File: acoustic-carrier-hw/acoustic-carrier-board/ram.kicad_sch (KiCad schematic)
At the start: 15 parts, among them IC1 ECP5-BGA256, IC2 MT41K256M16TW-107_P

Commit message: [carrier] Fixed minor symbol errors, added minor routing info (next) continue schematic check
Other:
- moved on the sheet: R54
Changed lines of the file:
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@@
 	(wire
 		(pts
-			(xy 223.52 68.58) (xy 227.33 68.58)
+			(xy 223.52 68.58) (xy 228.6 68.58)
 		)
 		(stroke
@@
 	(wire
 		(pts
-			(xy 232.41 68.58) (xy 240.03 68.58)
+			(xy 233.68 68.58) (xy 240.03 68.58)
 		)
 		(stroke
@@
 		(on_board yes)
 		(dnp no)
-		(fields_autoplaced yes)
 		(property "Reference" "IC1"
-			(at 90.17 76.6942 0)
+			(at 97.282 85.598 0)
 			(effects
 				(font
@@
 		)
 		(property "Value" "ECP5-BGA256"
-			(at 90.17 79.2342 0)
+			(at 106.426 88.392 0)
 			(effects
 				(font
@@
 	(symbol
 		(lib_id "Device:R_Small")
-		(at 229.87 68.58 90)
+		(at 231.14 68.58 90)
 		(unit 1)
 		(exclude_from_sim no)
@@
 		(dnp no)
 		(property "Reference" "R54"
-			(at 229.362 70.612 90)
+			(at 230.632 70.612 90)
 			(effects
 				(font
@@
 		)
 		(property "Value" "240"
-			(at 225.806 69.85 90)
+			(at 227.076 69.85 90)
 			(effects
 				(font
@@
 		)
 		(property "Footprint" "Resistor_SMD:R_0603_1608Metric"
-			(at 229.87 68.58 0)
+			(at 231.14 68.58 0)
 			(effects
 				(font
@@
 			)
 		)
-		(property "Datasheet" "~"
-			(at 229.87 68.58 0)
+		(property "Datasheet" "https://jlcpcb.com/api/file/downloadByFileSystemAccessId/8579706336479019008"
+			(at 231.14 68.58 0)
 			(effects
 				(font
@@
 		)
 		(property "Description" "Resistor, small symbol"
-			(at 229.87 68.58 0)
+			(at 231.14 68.58 0)
 			(effects
 				(font
@@
 		)
 		(property "LPN" "0603WAF2400T5E"
-			(at 229.87 68.58 0)
+			(at 231.14 68.58 0)
 			(effects
 				(font
@@
 		)
 		(property "MPN" "C23350"
-			(at 229.87 68.58 0)
-			(effects
-				(font
-					(size 1.27 1.27)
-				)
-				(hide yes)
-			)
-		)
-		(property "Part Number" ""
-			(at 229.87 68.58 90)
-			(effects
-				(font
-					(size 1.27 1.27)
-				)
-				(hide yes)
-			)
-		)
-		(property "SN-DK" ""
-			(at 229.87 68.58 90)
-			(effects
-				(font
-					(size 1.27 1.27)
-				)
-				(hide yes)
-			)
-		)
-		(property "Sim.Pin" ""
-			(at 229.87 68.58 90)
-			(effects
-				(font
-					(size 1.27 1.27)
-				)
-				(hide yes)
-			)
-		)
-		(property "LCSC Part" ""
-			(at 229.87 68.58 90)
+			(at 231.14 68.58 0)
 			(effects
 				(font

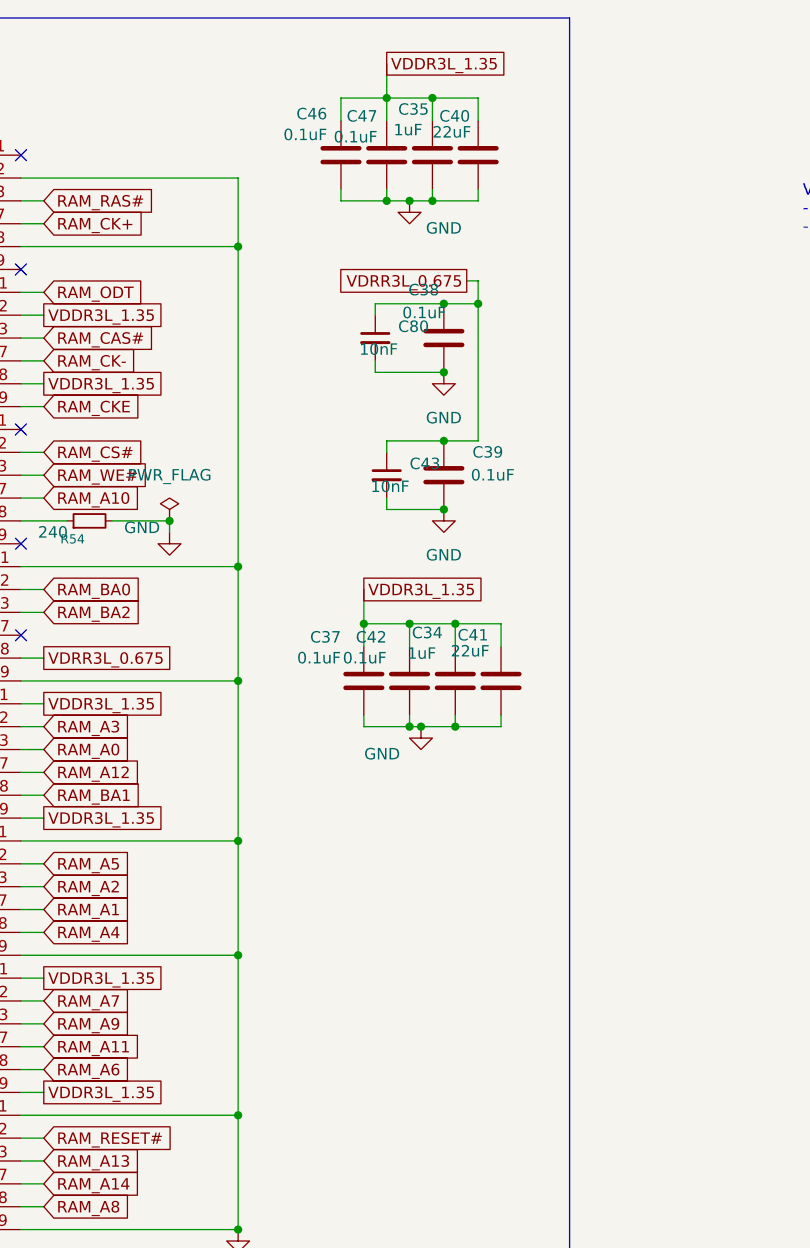
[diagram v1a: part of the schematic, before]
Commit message: [carrier] Finished flash and config check
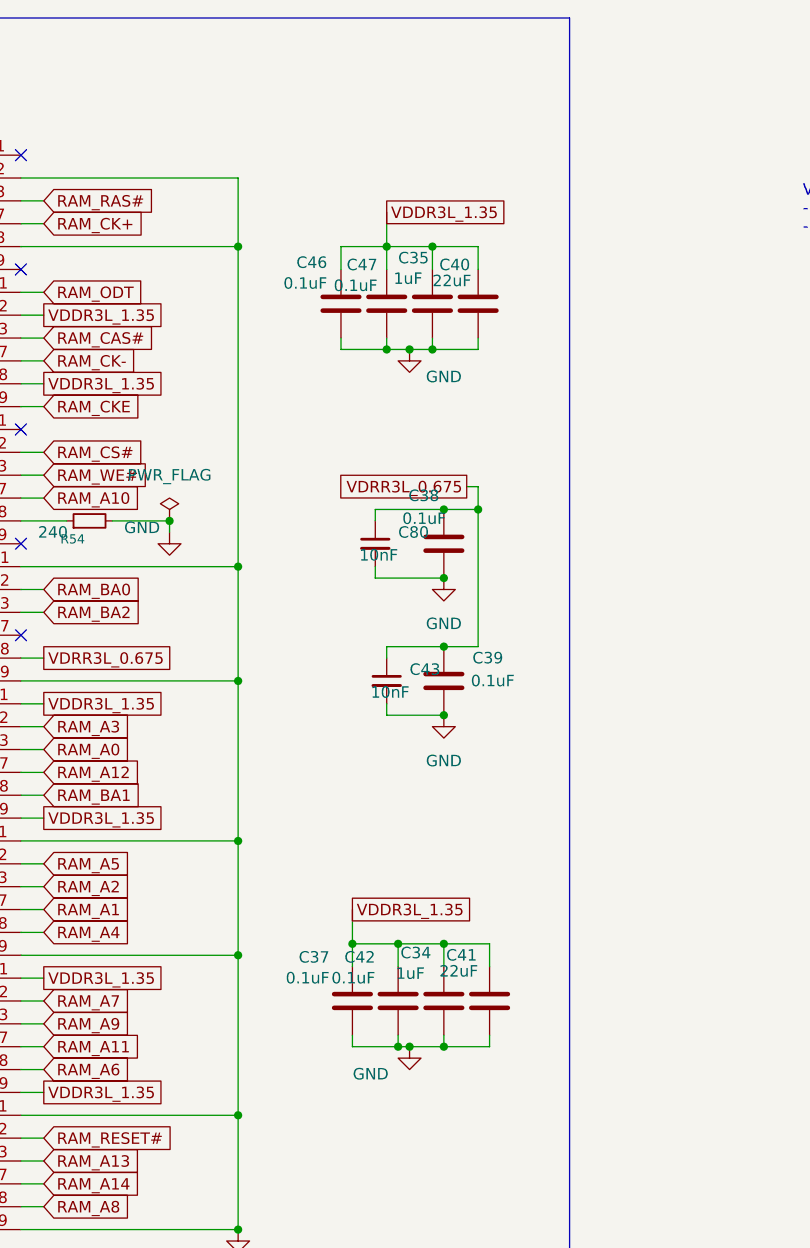
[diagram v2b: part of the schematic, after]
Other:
- moved on the sheet: C34, C35, C37, C38, C39, C40, C41, C42, C43, C46, C47, C80

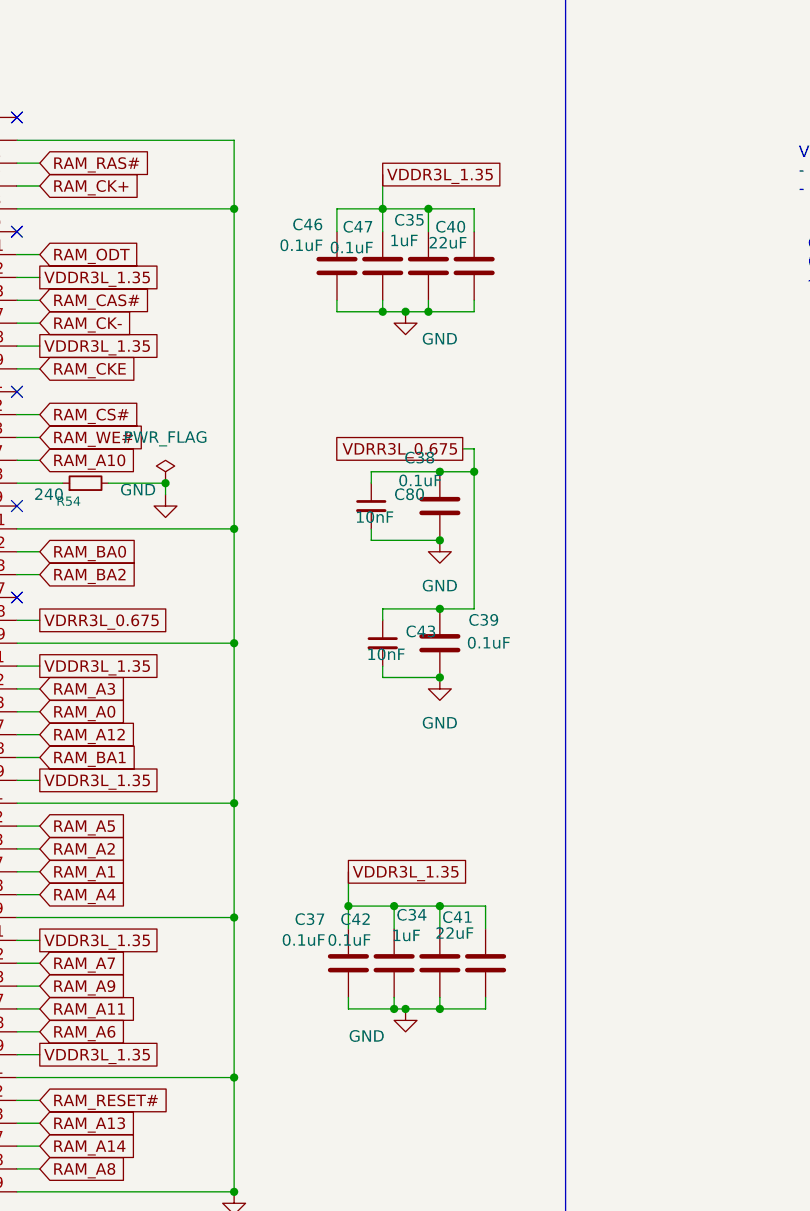
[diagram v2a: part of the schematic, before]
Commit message: [carrier] Further verification of power board (next) Replace ddr3l reference voltage using TPS51200
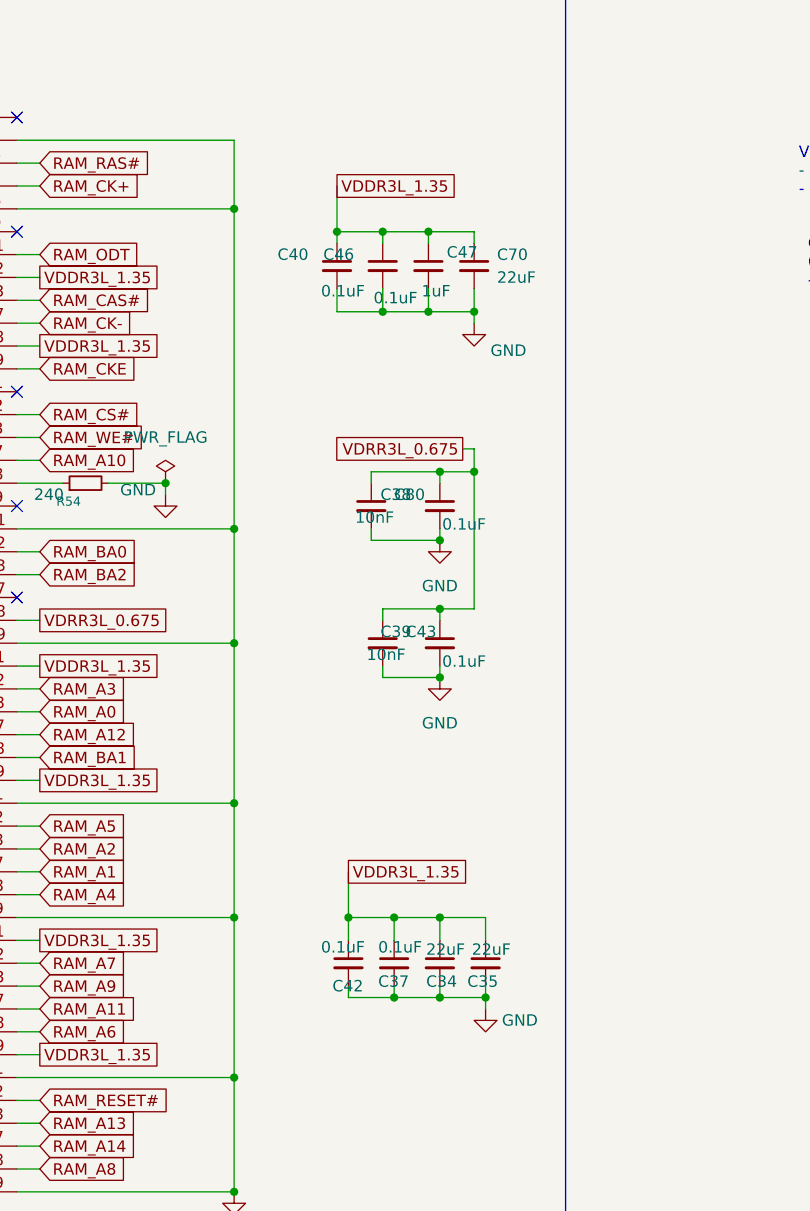
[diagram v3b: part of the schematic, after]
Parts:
- removed C34, C35: 1uF, Capacitor_SMD:C_0805_2012Metric, symbol Device:C
- removed C37, C38, C39, C42, C46, C47: 0.1uF, Capacitor_SMD:C_0402_1005Metric, symbol Device:C
- removed C40, C41: 22uF, Capacitor_SMD:C_0603_1608Metric, symbol Device:C
- added C34, C35, C70: 22uF, Capacitor_SMD:C_0603_1608Metric, symbol Device:C_Small
- added C37, C38, C39, C40, C42, C46: 0.1uF, Capacitor_SMD:C_0402_1005Metric, symbol Device:C_Small
- added C47: 1uF, Capacitor_SMD:C_0805_2012Metric, symbol Device:C_Small
- IC2: Height 1.2 -> (none); Manufacturer_Name Micron -> (none); Manufacturer_Part_Number MT41K256M16TW-107:P -> (none); Mouser Part Number 340-265846-TRAY -> (none); Mouser Price/Stock https://www.mouser.co.uk/ProductDetail/Micron/MT41K256M16TW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 -> (none)
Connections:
- net GND: now also C34.2, C35.2, C37.2, C38.2, C39.2, C40.2, C42.2, C46.2, C47.2, C70.2
- net VDDR3L_1.35: now also C34.1, C35.1, C37.1, C40.1, C42.1, C46.1, C47.1, C70.1
- net VDRR3L_0.675: now also C38.1, C39.1

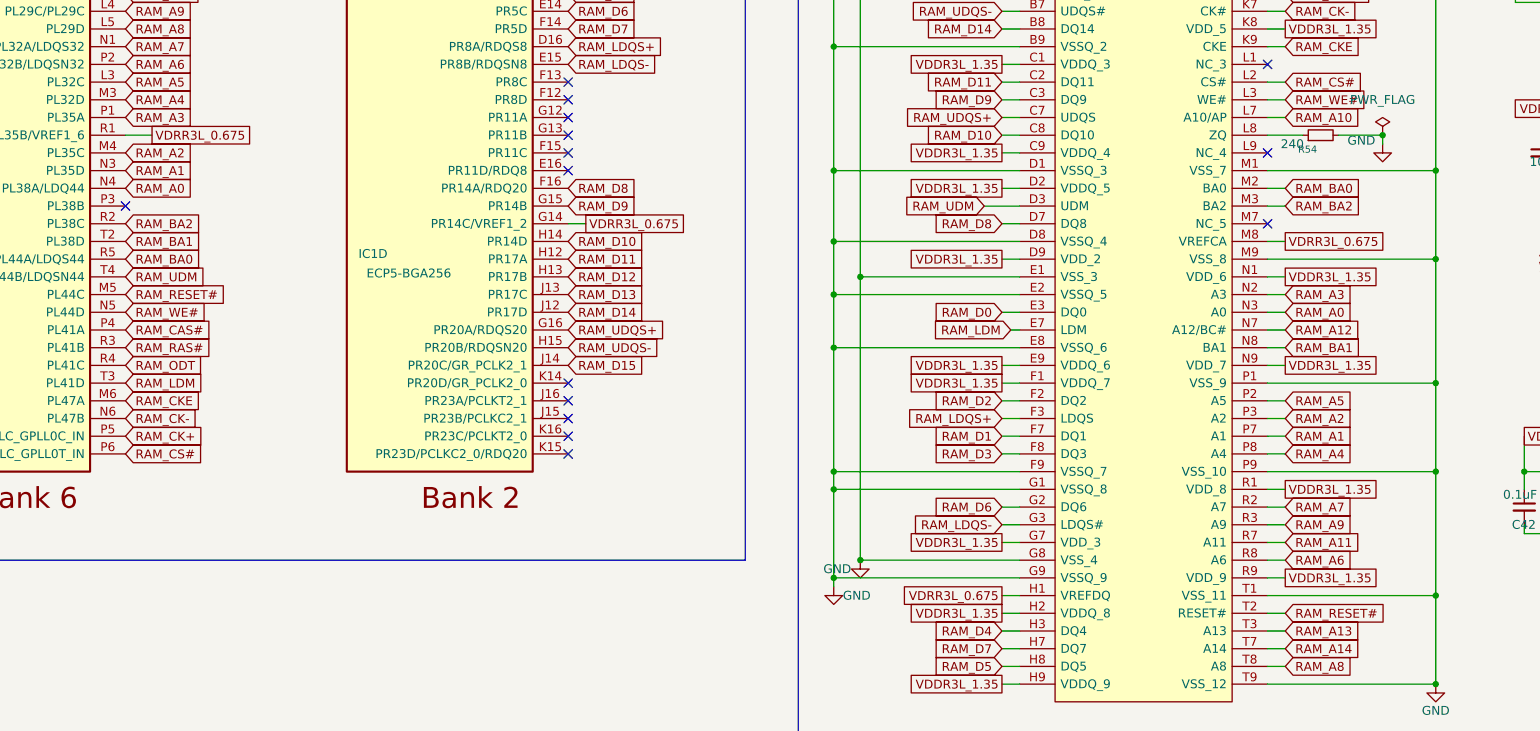
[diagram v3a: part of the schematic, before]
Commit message: [carrier] Added precision amplifier for DDRL voltage reference
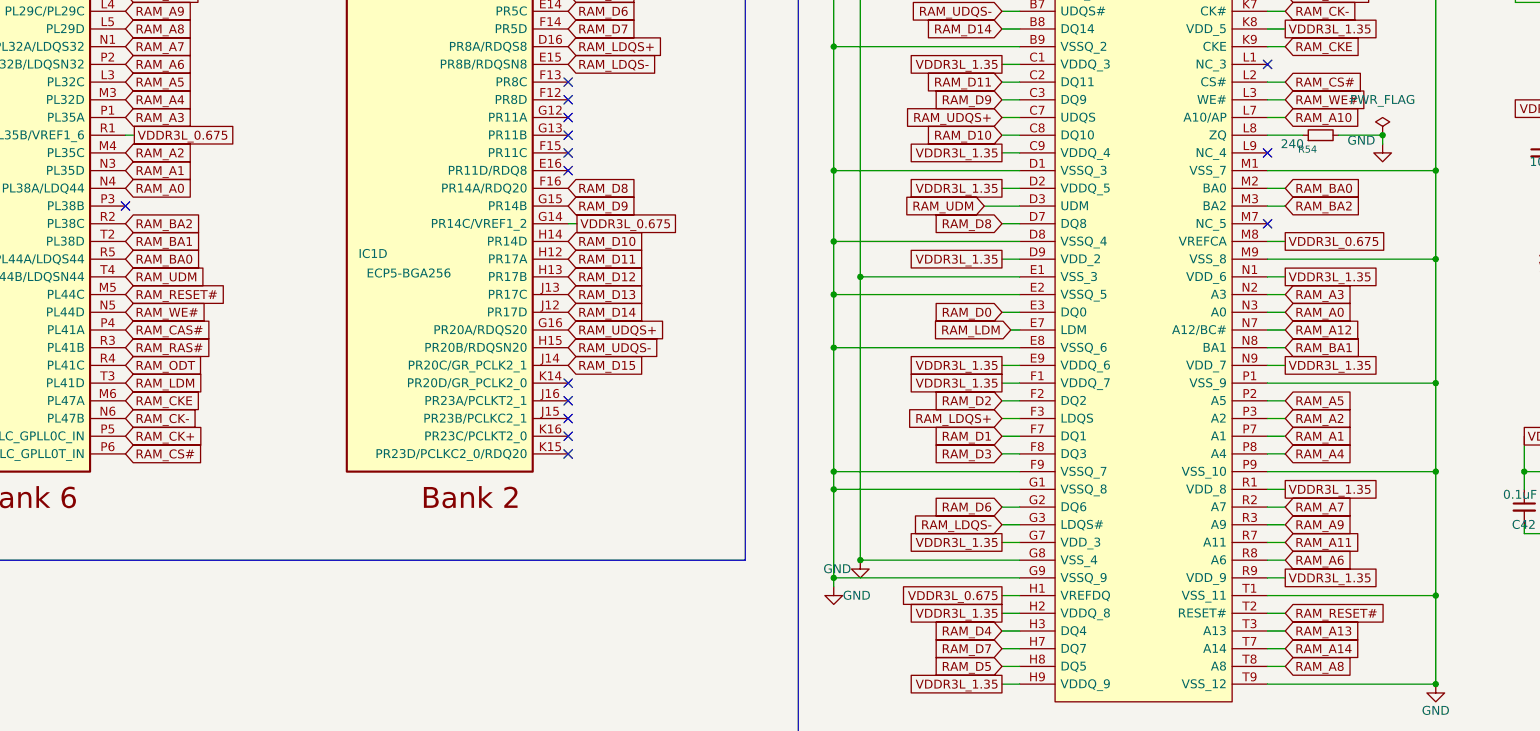
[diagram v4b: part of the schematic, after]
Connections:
- net VDRR3L_0.675: no longer IC1.G14 (PR14C/VREF1_2), IC1.R1 (PL35B/VREF1_6), IC2.H1 (VREFDQ), IC2.M8 (VREFCA)
- new net VDDR3L_0.675: IC1.G14 (PR14C/VREF1_2), IC1.R1 (PL35B/VREF1_6), IC2.H1 (VREFDQ), IC2.M8 (VREFCA)
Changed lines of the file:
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@@
 	(wire
 		(pts
-			(xy 63.5 68.58) (xy 59.69 68.58)
+			(xy 60.96 68.58) (xy 59.69 68.58)
 		)
 		(stroke
@@
 	(wire
 		(pts
-			(xy 123.19 81.28) (xy 125.73 81.28)
+			(xy 123.19 81.28) (xy 124.46 81.28)
 		)
 		(stroke
@@
 		)
 	)
-	(global_label "VDRR3L_0.675"
+	(global_label "VDDR3L_0.675"
 		(shape passive)
-		(at 226.06 83.82 0)
+		(at 124.46 81.28 0)
 		(fields_autoplaced yes)
 		(effects
@@
 		)
 		(property "Intersheetrefs" "${INTERSHEET_REFS}"
-			(at 241.4805 83.82 0)
+			(at 139.8805 81.28 0)
 			(effects
 				(font
@@
 		)
 	)
-	(global_label "VDRR3L_0.675"
-		(shape passive)
-		(at 125.73 81.28 0)
-		(fields_autoplaced yes)
-		(effects
-			(font
-				(size 1.27 1.27)
-			)
-			(justify left)
-		)
-		(property "Intersheetrefs" "${INTERSHEET_REFS}"
-			(at 141.1505 81.28 0)
-			(effects
-				(font
-					(size 1.27 1.27)
-				)
-				(justify left)
-				(hide yes)
-			)
-		)
-	)
 	(global_label "RAM_A10"
 		(shape input)
@@
 		)
 	)
-	(global_label "RAM_LDQS-"
-		(shape input)
-		(at 123.19 58.42 0)
+	(global_label "VDDR3L_0.675"
+		(shape passive)
+		(at 226.06 83.82 0)
+		(fields_autoplaced yes)
 		(effects
 			(font
@@
 		)
 		(property "Intersheetrefs" "${INTERSHEET_REFS}"
-			(at 123.19 58.42 0)
+			(at 241.4805 83.82 0)
 			(effects
 				(font
 					(size 1.27 1.27)
 				)
+				(justify left)
 				(hide yes)
 			)
 		)
 	)
-	(global_label "VDRR3L_0.675"
-		(shape passive)
-		(at 63.5 68.58 0)
-		(fields_autoplaced yes)
+	(global_label "RAM_LDQS-"
+		(shape input)
+		(at 123.19 58.42 0)
 		(effects
 			(font
@@
 		)
 		(property "Intersheetrefs" "${INTERSHEET_REFS}"
-			(at 78.9205 68.58 0)
+			(at 123.19 58.42 0)
 			(effects
 				(font
 					(size 1.27 1.27)
 				)
-				(justify left)
 				(hide yes)
 			)
@@
 		)
 	)
+	(global_label "VDDR3L_0.675"
+		(shape passive)
+		(at 185.42 134.62 180)
+		(fields_autoplaced yes)
+		(effects
+			(font
+				(size 1.27 1.27)
+			)
+			(justify right)
+		)
+		(property "Intersheetrefs" "${INTERSHEET_REFS}"
+			(at 169.9995 134.62 0)
+			(effects
+				(font
+					(size 1.27 1.27)
+				)
+				(justify right)
+				(hide yes)
+			)
+		)
+	)
 	(global_label "RAM_UDM"
 		(shape input)
@@
 		)
 	)
-	(global_label "VDRR3L_0.675"
-		(shape passive)
-		(at 185.42 134.62 180)
-		(fields_autoplaced yes)
-		(effects
-			(font
-				(size 1.27 1.27)
-			)
-			(justify right)
-		)
-		(property "Intersheetrefs" "${INTERSHEET_REFS}"
-			(at 169.9995 134.62 0)
-			(effects
-				(font
-					(size 1.27 1.27)
-				)
-				(justify right)
-				(hide yes)
-			)
-		)
-	)
 	(global_label "RAM_A13"
 		(shape input)
@@
 				(hide yes)
 			)
+		)
+	)
+	(global_label "VDDR3L_0.675"
+		(shape passive)
+		(at 60.96 68.58 0)
+		(fields_autoplaced yes)
+		(effects
+			(font
+				(size 1.27 1.27)
+			)
+			(justify left)
+		)
+		(property "Intersheetrefs" "${INTERSHEET_REFS}"
+			(at 76.3805 68.58 0)
+			(effects
+				(font
+					(size 1.27 1.27)
+				)
+				(justify left)
+				(hide yes)
+			)
